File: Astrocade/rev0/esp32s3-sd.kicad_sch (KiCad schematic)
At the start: 15 parts, among them J2 microSD, SW3 RESET, SW4 BOOT, U2 ESP32-S3-WROOM-1-N16R8

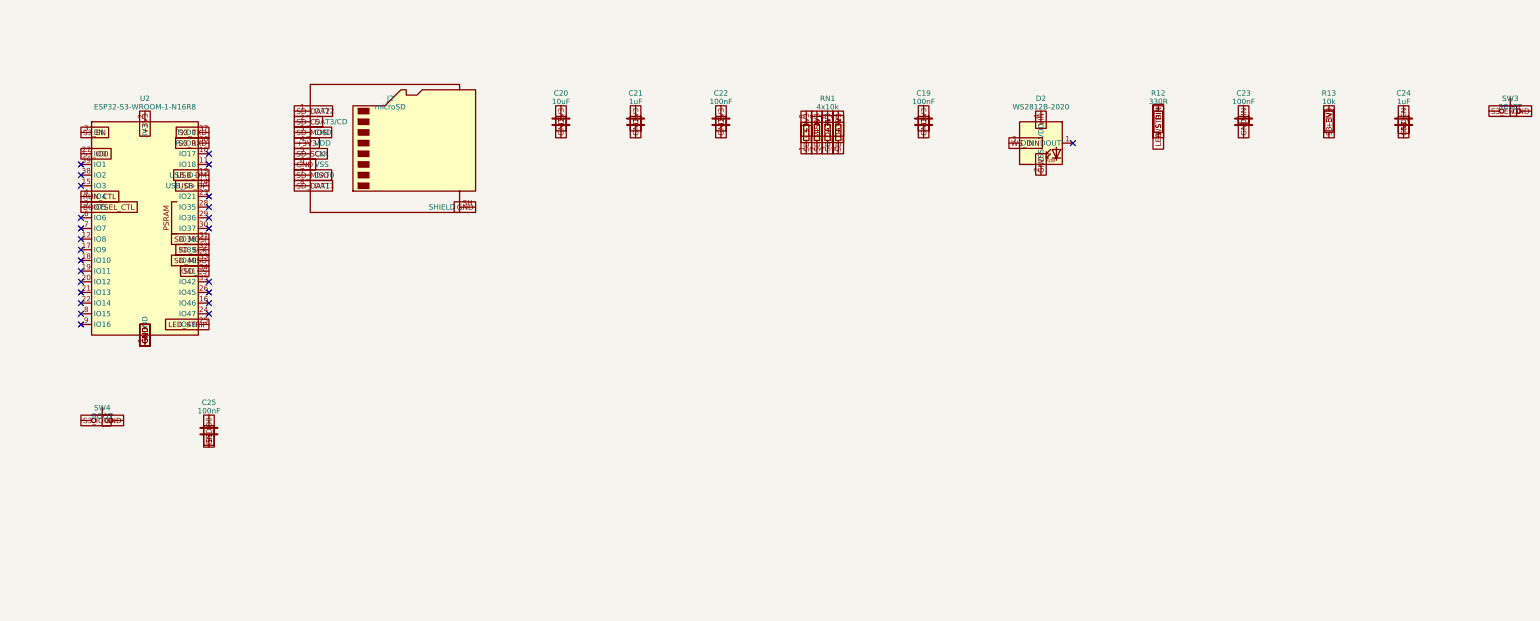
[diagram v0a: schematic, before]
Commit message: Astrocade Rev0: redo on RP2354A + ESP32-S3, 6-layer, fully autorouted
Replaces the unrouted RP2040 + 3x LVC245 draft with an INTV-style board:
RP2354A straight on the 5V bus, ESP32-S3-WROOM-1-N16R8 as its USB host
(PICOBOOT reflash), USB-C/CP2102N, push-push microSD, WS2812B-2020-V6,
RESET/BOOTSEL/EN/BOOT buttons. Same cassette outline, lands and holes.

Everything is generated by tools/ (build_all.sh): design.py -> schematic,
placement + plane fan-out, Raspberry Pi's MIT regulator-corner graft,
Freerouting + A* finisher, netlist-vs-firmware check, JLCPCB BOM/CPL/gerbers.
ERC 0, DRC 0 errors / 0 unconnected / 0 parity, check_nets 174/174.

RUN/BOOTSEL from the S3 are direct 1k links (fnPicoUpdater drives them low;
an NPN driver would invert it). Shell openings come from the placement.

Co-Authored-By: Claude Opus 5.5 (1M context) <noreply@anthropic.com>
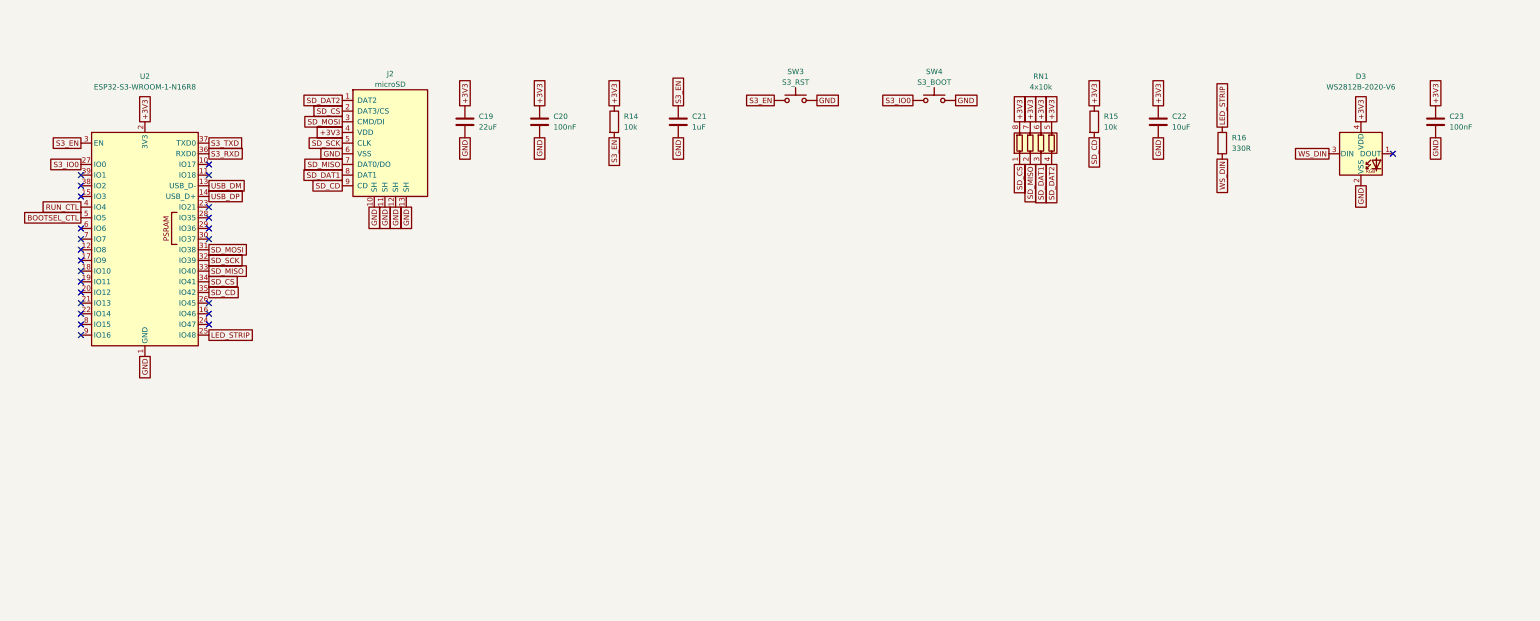
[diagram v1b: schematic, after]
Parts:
- removed C24: 1uF, FujiNet-Astrocade:C_0603_1608Metric, symbol Device:C
- removed C25: 100nF, FujiNet-Astrocade:C_0603_1608Metric, symbol Device:C
- removed D2: WS2812B-2020, FujiNet-Astrocade:LED_WS2812B-2020_PLCC4_2.0x2.0mm, symbol LED:WS2812B-2020
- removed J2: microSD, FujiNet-Astrocade:microSD_SUNTECH_ST-TF-003A, symbol Connector:Micro_SD_Card
- removed R12: 330R, FujiNet-Astrocade:R_0603_1608Metric, symbol Device:R
- removed R13: 10k, FujiNet-Astrocade:R_0603_1608Metric, symbol Device:R
- added D3: WS2812B-2020-V6, FujiNet-Astrocade:LED_WS2812B-2020_PLCC4_2.0x2.0mm, symbol LED:WS2812B-2020
- added J2: microSD, FujiNet-Astrocade:TF-SMD_TF-015, symbol FujiNet-Astrocade:MicroSD_TF015
- added R14, R15: 10k, FujiNet-Astrocade:R_0603_1608Metric, symbol Device:R
- added R16: 330R, FujiNet-Astrocade:R_0603_1608Metric, symbol Device:R
- C19: value 100nF -> 22uF; footprint FujiNet-Astrocade:C_0603_1608Metric -> FujiNet-Astrocade:C_0805_2012Metric; LCSC (none) -> C45783; MPN (none) -> CL21A226MAQNNNE
- C20: value 10uF -> 100nF; LCSC C19702 -> C14663; MPN (none) -> CC0603KRX7R9BB104
- C21: LCSC (none) -> C15849; MPN (none) -> CL10A105KB8NNNC
- C22: value 100nF -> 10uF; LCSC (none) -> C19702; MPN (none) -> CL10A106KP8NNNC
- C23: LCSC (none) -> C14663; MPN (none) -> CC0603KRX7R9BB104
- RN1: LCSC (none) -> C29718; MPN (none) -> 4D03WGJ0103T5E
- SW3: value RESET -> S3_RST; LCSC (none) -> C2886898; MPN (none) -> TL3342F160QG
- SW4: value BOOT -> S3_BOOT; LCSC (none) -> C2886898; MPN (none) -> TL3342F160QG
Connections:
- net VIN is gone; now on net +3V3: C23.1
- net +3V3: now also D3.4 (VDD), J2.4 (VDD), R14.1, R15.1; no longer C21.1
- net GND: now also D3.2 (VSS), J2.10 (SH), J2.11 (SH), J2.12 (SH), J2.13 (SH), J2.6 (VSS)
- net LED_STRIP: now also R16.1
- net S3_EN: now also C21.1, R14.2
- net SD_CS: now also J2.2 (DAT3/CS)
- net SD_DAT1: now also J2.8 (DAT1)
- net SD_DAT2: now also J2.1 (DAT2)
- net SD_MISO: now also J2.7 (DAT0/DO)
- net SD_MOSI: now also J2.3 (CMD/DI)
- net SD_SCK: now also J2.5 (CLK)
- net WS_DIN: now also D3.3 (DIN), R16.2
- net SD_CD: now reaches U2.35 (IO42)
- net SD_CD: now also J2.9 (CD), R15.2
- no-connect marks 25 -> 24
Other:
- company: (none) -> FujiNet
- title: (none) -> FujiNet Astrocade Rev0 - ESP32-S3 FujiNet core, microSD, status LED

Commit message: Astrocade Rev0: audit with kicad-happy + datasheets and redo
Schematic, board and fab outputs regenerated from tools/ after a
datasheet-level audit (docs/design-review-rev0.md).

Design fixes:
- RP2354A on its own AP2112K rail (+3V3_RP): its FT pads take 5.5 V only
  with IOVDD powered (RP2350 DS p.1332); the buck's UVLO + 4 ms soft-start
  left them unpowered while the console drove the bus
- WS2812B-2020-V6 on +5V (datasheet VDD 3.7-5.3 V, not a 3.3 V part)
- VBUS decoupling at the USB-C, activity LED 330R, card-detect polarity
  settled (low = card present), fiducials, RUN/BOOTSEL/rail test pads

Schematic redrawn readably: root block diagram with hierarchical pins,
power symbols, wired clusters and design notes (tools/sch_layout.py);
check_sch_layout.py proves the drawn netlist equals design.py.

Board: 4 layers tried first and did not close; 6 layers, 100% routed,
DRC 0 errors / 0 unconnected / 0 parity. Locked USB-C D+/D- pad ties,
GND stitching kept out of pads, return vias at USB/crystal layer
changes, check_vias.py gate (KiCad re-nets a via inside another net's
pad, so its DRC cannot see it).

Co-Authored-By: Claude Opus 5.5 <noreply@anthropic.com>
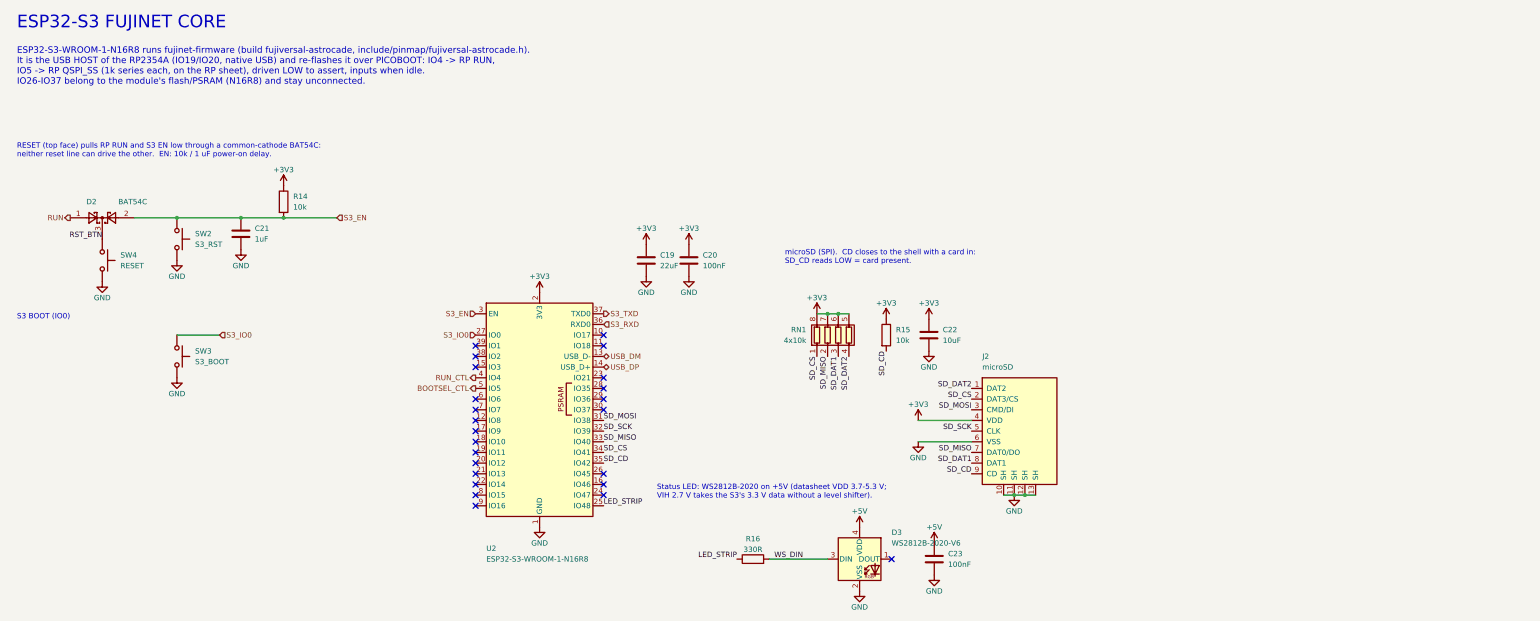
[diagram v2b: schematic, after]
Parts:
- added D2: BAT54C, FujiNet-Astrocade:SOT-23, symbol Diode:BAT54C
- added SW2: S3_RST, FujiNet-Astrocade:SW_SPST_TL3342, symbol Switch:SW_Push
- SW3: value S3_RST -> S3_BOOT
- SW4: value S3_BOOT -> RESET
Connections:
- net +3V3: no longer C23.1, D3.4 (VDD)
- net GND: now also SW2.2
- net S3_EN: now also D2.2, SW2.1; no longer SW3.1
- net S3_IO0: now also SW3.1; no longer SW4.1
- new net +5V: C23.1, D3.4 (VDD)
- new net RST_BTN: D2.3, SW4.1
- new net RUN: D2.1
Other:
- note added: "ESP32-S3 FUJINET CORE"
- note added: "ESP32-S3-WROOM-1-N16R8 runs fujinet-firmware (build fujiversal-astrocade, include/pinmap/fujiversal-astrocade.h). It is the USB HOST of the RP2354A (IO19/IO20, native USB) and re-flashes it over PICOBOOT: IO4 -> RP RUN, IO5 -> RP QSPI_SS (1k series each, on the RP sheet), driven LOW to assert, inputs when idle. IO26-IO37 belong to the module's flash/PSRAM (N16R8) and stay unconnected."
- note added: "RESET (top face) pulls RP RUN and S3 EN low through a common-cathode BAT54C: neither reset line can drive the other. EN: 10k / 1 uF power-on delay."
- note added: "S3 BOOT (IO0)"
- note added: "Status LED: WS2812B-2020 on +5V (datasheet VDD 3.7-5.3 V; VIH 2.7 V takes the S3's 3.3 V data without a level shifter)."
- note added: "microSD (SPI). CD closes to the shell with a card in: SD_CD reads LOW = card present."
- title: FujiNet Astrocade Rev0 - ESP32-S3 FujiNet core, microSD, status LED -> FujiNet Astrocade Rev0 - ESP32-S3 FujiNet core, microSD, status LED, RESET
- moved on the sheet: C19, C20, C21, C22, C23, D3, J2, R14, R15, R16, RN1, SW3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
